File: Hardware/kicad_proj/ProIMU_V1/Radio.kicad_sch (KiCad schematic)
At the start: 3 parts, among them U6 AIR602, U7 L80-M39

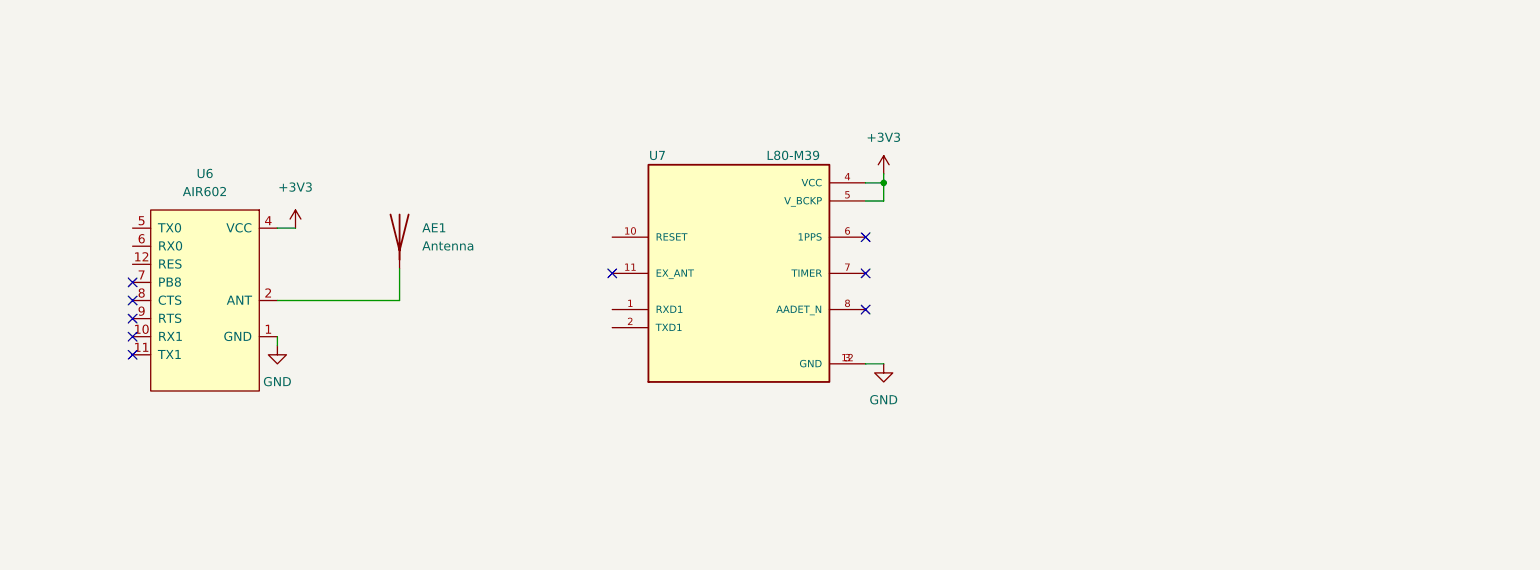
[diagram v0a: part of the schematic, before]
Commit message: Added a completed GPS V1 Schematic
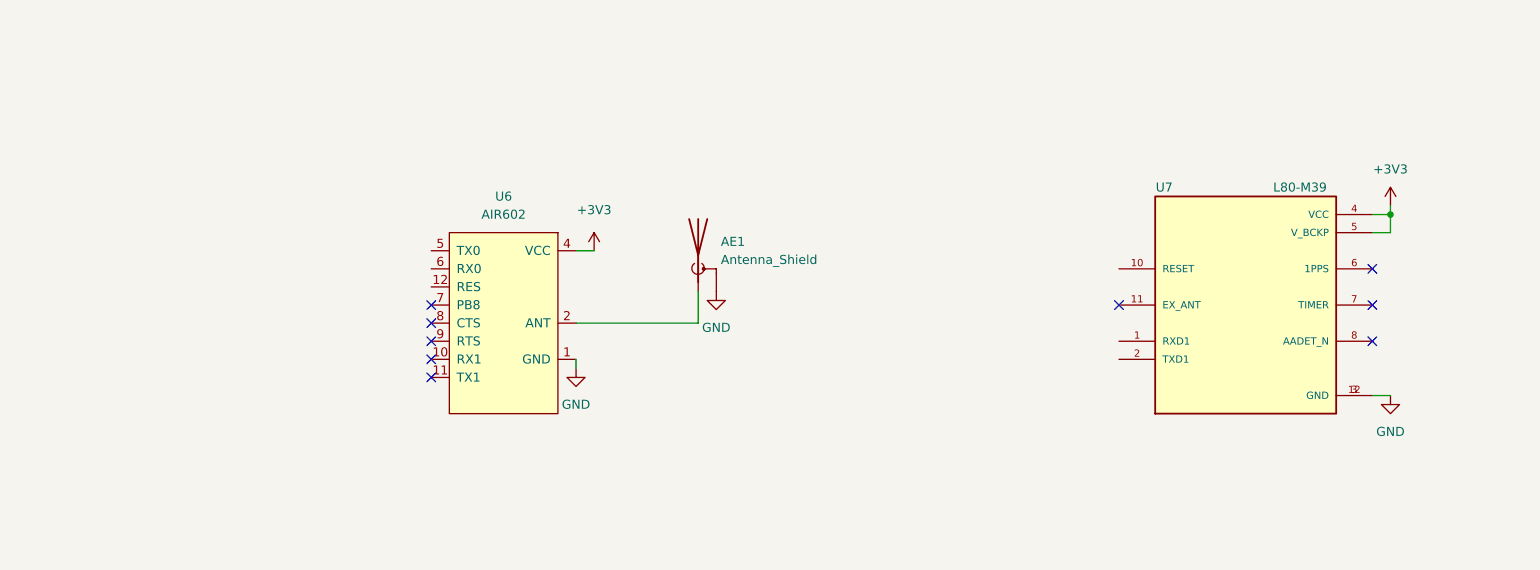
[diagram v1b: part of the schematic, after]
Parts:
- removed AE1: Antenna, RF_Antenna:Texas_SWRA117D_2.4GHz_Left, symbol Device:Antenna
- added AE1: Antenna_Shield, RF_Antenna:Texas_SWRA117D_2.4GHz_Left, symbol Device:Antenna_Shield
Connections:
- net GND: now also AE1.2 (Shield)
- net at U6.2 (ANT): now also AE1.1 (A)
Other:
- moved on the sheet: U6, U7

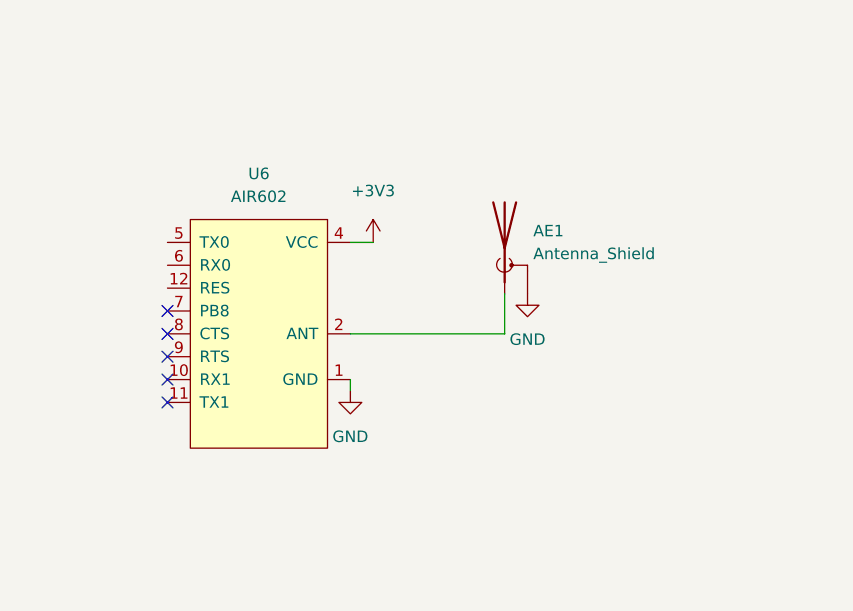
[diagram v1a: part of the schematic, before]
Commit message: Added GPS, LoRa and Wifi v1 schematic blocks
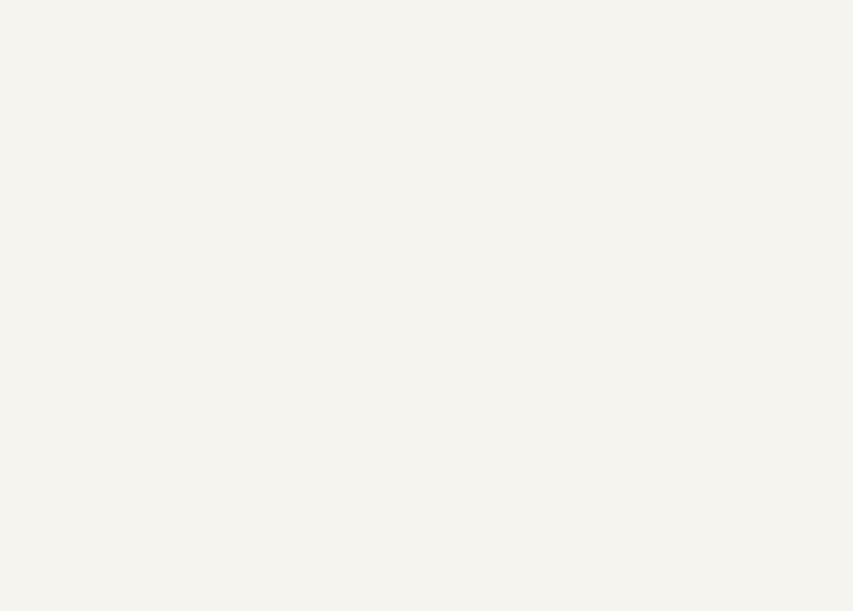
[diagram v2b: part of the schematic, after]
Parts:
- removed AE1: Antenna_Shield, RF_Antenna:Texas_SWRA117D_2.4GHz_Left, symbol Device:Antenna_Shield
- removed U6: AIR602, footprints:AIR602, symbol air602:AIR602
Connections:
- no-connect marks 9 -> 4
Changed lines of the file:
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@@
   (no_connect (at 218.44 65.405))
   (no_connect (at 182.88 60.325))
-  (no_connect (at 86.36 62.865))
-  (no_connect (at 86.36 70.485))
-  (no_connect (at 86.36 65.405))
-  (no_connect (at 86.36 67.945))
-  (no_connect (at 86.36 60.325))
   (no_connect (at 218.44 60.325))
-  (wire (pts (xy 106.68 62.865) (xy 123.825 62.865))
-    (stroke (width 0) (type default) (color 0 0 0 0))
-  )
   (polyline (pts (xy 284.48 12.7) (xy 284.48 102.87))
     (stroke (width 0) (type default) (color 0 0 0 0))
@@
     (stroke (width 0) (type default) (color 0 0 0 0))
   )
-  (wire (pts (xy 109.22 52.705) (xy 106.68 52.705))
-    (stroke (width 0) (type default) (color 0 0 0 0))
-  )
   (wire (pts (xy 218.44 73.025) (xy 220.98 73.025))
     (stroke (width 0) (type default) (color 0 0 0 0))
@@
     (stroke (width 0) (type default) (color 0 0 0 0))
   )
-  (wire (pts (xy 123.825 58.42) (xy 123.825 62.865))
-    (stroke (width 0) (type default) (color 0 0 0 0))
-  )
   (polyline (pts (xy 284.48 102.87) (xy 12.7 102.87))
     (stroke (width 0) (type default) (color 0 0 0 0))
@@
   )
   (wire (pts (xy 218.44 47.625) (xy 220.98 47.625))
-    (stroke (width 0) (type default) (color 0 0 0 0))
-  )
-  (wire (pts (xy 106.68 67.945) (xy 106.68 69.215))
     (stroke (width 0) (type default) (color 0 0 0 0))
   )
@@
     (pin "1")
   )
-  (symbol (lib_id "power:+3V3") (at 109.22 52.705 0) (mirror y) (unit 1)
-    (in_bom yes) (on_board yes) (fields_autoplaced)
-    (property "Reference" "#PWR049" (id 0) (at 109.22 56.515 0)
-      (effects (font (size 1.27 1.27)) hide)
-    )
-    (property "Value" "+3V3" (id 1) (at 109.22 46.99 0))
-    (property "Footprint" "" (id 2) (at 109.22 52.705 0)
-      (effects (font (size 1.27 1.27)) hide)
-    )
-    (property "Datasheet" "" (id 3) (at 109.22 52.705 0)
-      (effects (font (size 1.27 1.27)) hide)
-    )
-    (pin "1")
-  )
-  (symbol (lib_id "power:GND") (at 106.68 69.215 0) (mirror y) (unit 1)
-    (in_bom yes) (on_board yes) (fields_autoplaced)
-    (property "Reference" "#PWR048" (id 0) (at 106.68 75.565 0)
-      (effects (font (size 1.27 1.27)) hide)
-    )
-    (property "Value" "GND" (id 1) (at 106.68 74.295 0))
-    (property "Footprint" "" (id 2) (at 106.68 69.215 0)
-      (effects (font (size 1.27 1.27)) hide)
-    )
-    (property "Datasheet" "" (id 3) (at 106.68 69.215 0)
-      (effects (font (size 1.27 1.27)) hide)
-    )
-    (pin "1")
-  )
   (symbol (lib_id "power:+3V3") (at 220.98 46.355 0) (unit 1)
     (in_bom yes) (on_board yes) (fields_autoplaced)
@@
     )
     (property "Datasheet" "" (id 3) (at 220.98 46.355 0)
-      (effects (font (size 1.27 1.27)) hide)
-    )
-    (pin "1")
-  )
-  (symbol (lib_id "power:GND") (at 126.365 58.42 0) (mirror y) (unit 1)
-    (in_bom yes) (on_board yes) (fields_autoplaced)
-    (property "Reference" "#PWR053" (id 0) (at 126.365 64.77 0)
-      (effects (font (size 1.27 1.27)) hide)
-    )
-    (property "Value" "GND" (id 1) (at 126.365 63.5 0))
-    (property "Footprint" "" (id 2) (at 126.365 58.42 0)
-      (effects (font (size 1.27 1.27)) hide)
-    )
-    (property "Datasheet" "" (id 3) (at 126.365 58.42 0)
       (effects (font (size 1.27 1.27)) hide)
     )
@@
     (pin "8")
   )
-  (symbol (lib_id "air602:AIR602") (at 96.52 60.325 0) (mirror y) (unit 1)
-    (in_bom yes) (on_board yes) (fields_autoplaced)
-    (property "Reference" "U6" (id 0) (at 96.52 45.085 0))
-    (property "Value" "AIR602" (id 1) (at 96.52 47.625 0))
-    (property "Footprint" "footprints:AIR602" (id 2) (at 96.52 60.325 0)
-      (effects (font (size 1.27 1.27)) hide)
-    )
-    (property "Datasheet" "" (id 3) (at 96.52 60.325 0)
-      (effects (font (size 1.27 1.27)) hide)
-    )
-    (pin "1")
-    (pin "10")
-    (pin "11")
-    (pin "12")
-    (pin "2")
-    (pin "3")
-    (pin "4")
-    (pin "5")
-    (pin "6")
-    (pin "7")
-    (pin "8")
-    (pin "9")
-  )
-  (symbol (lib_id "Device:Antenna_Shield") (at 123.825 53.34 0) (unit 1)
-    (in_bom yes) (on_board yes) (fields_autoplaced)
-    (property "Reference" "AE1" (id 0) (at 127 51.4349 0)
-      (effects (font (size 1.27 1.27)) (justify left))
-    )
-    (property "Value" "Antenna_Shield" (id 1) (at 127 53.9749 0)
-      (effects (font (size 1.27 1.27)) (justify left))
-    )
-    (property "Footprint" "RF_Antenna:Texas_SWRA117D_2.4GHz_Left" (id 2) (at 123.825 50.8 0)
-      (effects (font (size 1.27 1.27)) hide)
-    )
-    (property "Datasheet" "~" (id 3) (at 123.825 50.8 0)
-      (effects (font (size 1.27 1.27)) hide)
-    )
-    (pin "1")
-    (pin "2")
-  )
 )
